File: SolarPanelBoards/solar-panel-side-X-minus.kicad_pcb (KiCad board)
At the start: 2 copper layers, 82 x 99 mm, 24 parts, among them J1 Conn_01x06, U1 OPT3001DNPT

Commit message: rearranged x-minus
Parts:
- moved C1 25.4 mm to (149.1, 79.8)
- moved U1 25.4 mm to (154.2, 79.8)
- moved SC1 9.67 mm to (126.6, 61.4), turned to 90 degrees
- moved SC2 9.39 mm to (176.9, 61.1), turned to 90 degrees
- moved D5 6.47 mm to (113.1, 118.6)
- moved D4 5.96 mm to (189.3, 119.8)
- moved SC4 5.68 mm to (168.8, 120.0), turned to 180 degrees
- moved SC5 5.68 mm to (133.2, 120.0), turned to 0 degrees
- moved SC3 5.40 mm to (168.8, 97.5), turned to 180 degrees
- moved SC6 5.40 mm to (133.3, 97.5), turned to 0 degrees
- moved D9 5.32 mm to (140.2, 81.8)
- moved D1 4.57 mm to (143.5, 81.9)
- moved D2 4.17 mm to (163.2, 82.4)
- moved J1 1.47 mm to (124.8, 59.9)
- moved D3 1.39 mm to (189.4, 102.1)
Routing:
- net Net-(D4-Pad2): track 78.5 -> 17.0 mm
- net Net-(D3-Pad2): track 30.3 -> 91.9 mm
- net SCL: track 42.0 -> 4.28 mm
- net GND: track 0.65 -> 31.8 mm, vias 16 -> 12
- net +3V3: track 29.9 -> 4.14 mm, vias 1 -> 0
- net VSOLAR: track 58.8 -> 83.8 mm, vias 1 -> 2
- net Net-(D2-Pad2): track 37.1 -> 18.1 mm
- net SDA: track 38.6 -> 20.2 mm
- net Net-(D1-Pad1): track 14.9 -> 0.00 mm, vias 0 -> 4
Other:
- outline, holes or cut-outs redrawn
- net class Default removed

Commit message: new coils
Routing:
- net VSOLAR: track 83.8 -> 39658.4 mm, vias 2 -> 15
- net Net-(D4-Pad2): track 17.0 -> 33.4 mm
- net Net-(D3-Pad2): track 91.9 -> 83.5 mm
- net Net-(D5-Pad2): track 30.3 -> 22.2 mm
- net Net-(D1-Pad1): vias 4 -> 0
- net GND: vias 12 -> 6
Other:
- copper layers 2 -> 6

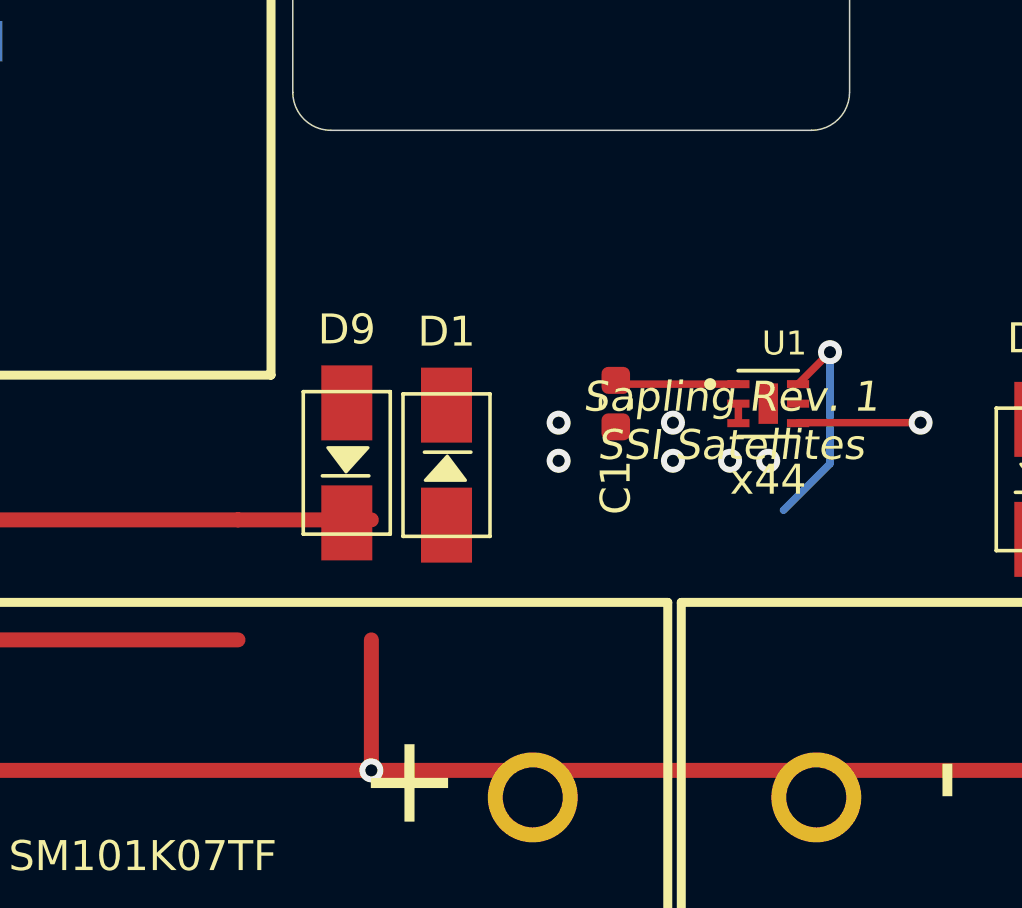
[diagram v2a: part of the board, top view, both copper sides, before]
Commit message: added I2C protection PCB layout
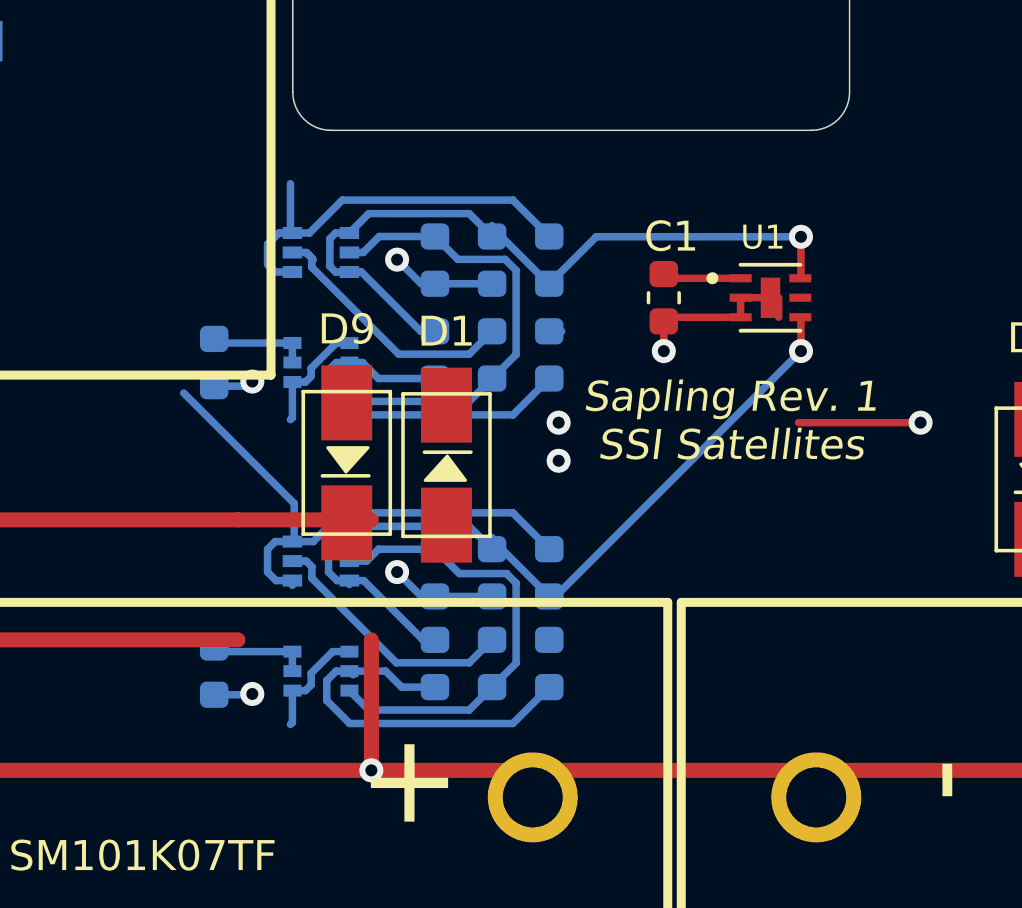
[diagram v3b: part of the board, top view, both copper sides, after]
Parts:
- added C2: 10nF, Capacitor_SMD:C_0603_1608Metric, B.Cu at (146.9, 88.5)
- added C3: 10nF, Capacitor_SMD:C_0603_1608Metric, B.Cu at (146.9, 78.2)
- added Q1: MBT2222ADW1T1, Package_TO_SOT_SMD:SOT-363_SC-70-6, B.Cu at (139.3, 85.1)
- added Q2: MBT2222ADW1T1, Package_TO_SOT_SMD:SOT-363_SC-70-6, B.Cu at (139.3, 74.8)
- added Q3: BSS138DWQ-7, mainboard:BSS138DWQ-7, B.Cu at (139.3, 88.8)
- added Q4: BSS138DWQ-7, mainboard:BSS138DWQ-7, B.Cu at (139.3, 78.5)
- added R1: 10K, Resistor_SMD:R_0603_1608Metric, B.Cu at (143.1, 85.5)
- added R10: 200K, Resistor_SMD:R_0603_1608Metric, B.Cu at (143.1, 78.2)
- added R11: 0, Resistor_SMD:R_0603_1608Metric, B.Cu at (146.9, 85.5)
- added R12: 0, Resistor_SMD:R_0603_1608Metric, B.Cu at (146.9, 75.1)
- added R2: 10K, Resistor_SMD:R_0603_1608Metric, B.Cu at (143.1, 75.1)
- added R3: 10K, Resistor_SMD:R_0603_1608Metric, B.Cu at (145.0, 85.5)
- added R4: 10K, Resistor_SMD:R_0603_1608Metric, B.Cu at (145.0, 75.1)
- added R5: 680, Resistor_SMD:R_0603_1608Metric, B.Cu at (145.0, 88.5)
- added R6: 680, Resistor_SMD:R_0603_1608Metric, B.Cu at (145.0, 78.2)
- added R7: 100K, Resistor_SMD:R_0603_1608Metric, B.Cu at (135.7, 88.8)
- added R8: 100K, Resistor_SMD:R_0603_1608Metric, B.Cu at (135.7, 78.5)
- added R9: 200K, Resistor_SMD:R_0603_1608Metric, B.Cu at (143.1, 88.5)
- moved C1 3.88 mm to (150.7, 76.3)
- moved U1 3.53 mm to (154.3, 76.3)
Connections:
- U1 pad 4: SCL -> (no net)
- U1 pad 6: SDA -> (no net)
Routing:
- net (no net): track 0.00 -> 135.0 mm, vias 0 -> 2
- net SCL: track 4.28 -> 23.2 mm
- net GND: track 31.8 -> 45.4 mm, vias 6 -> 3
- net +3V3: track 4.14 -> 13.5 mm, vias 0 -> 4
- net SDA: track 20.2 -> 26.6 mm, vias 1 -> 0
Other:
- board text added: "BYP"
- board text added: "DNP"
- board text removed: "x44"

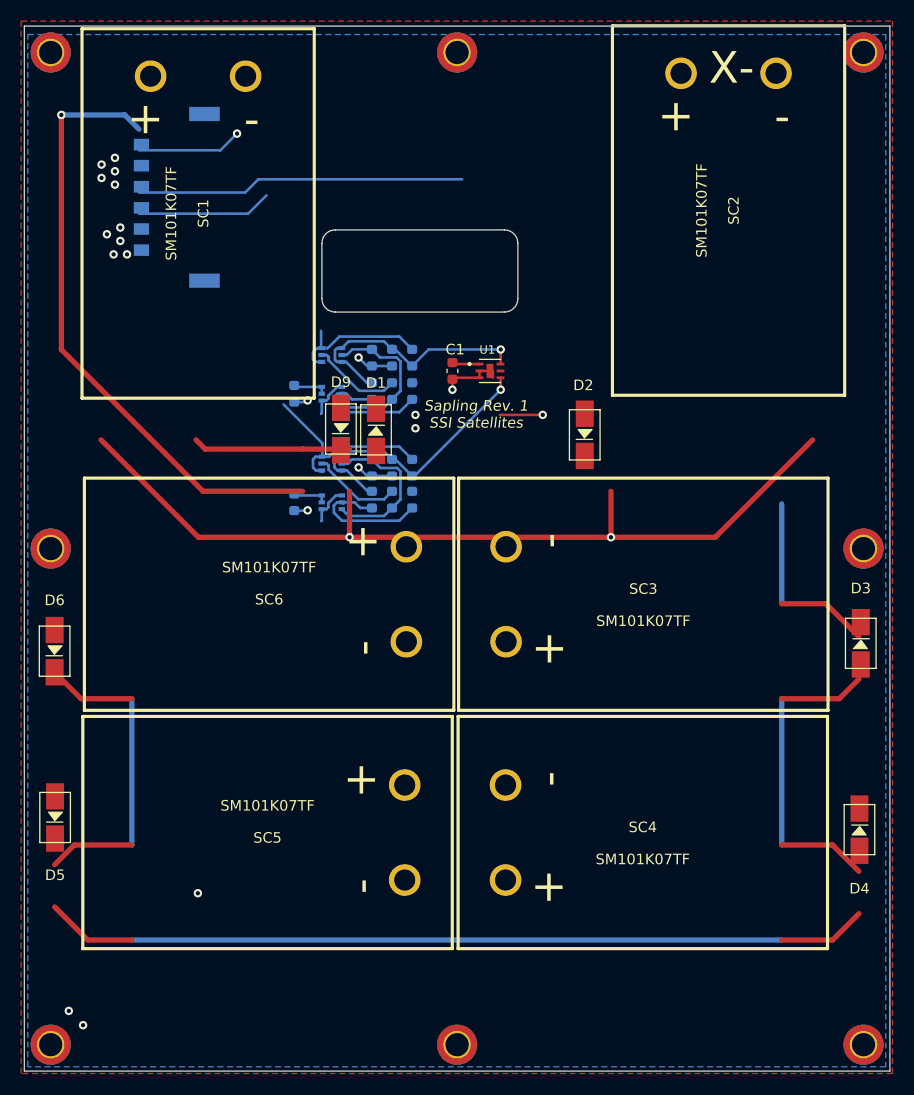
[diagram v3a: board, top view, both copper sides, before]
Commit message: New X-minus board w/ magnetorquer coils and H-bridge, I2C protection circuit
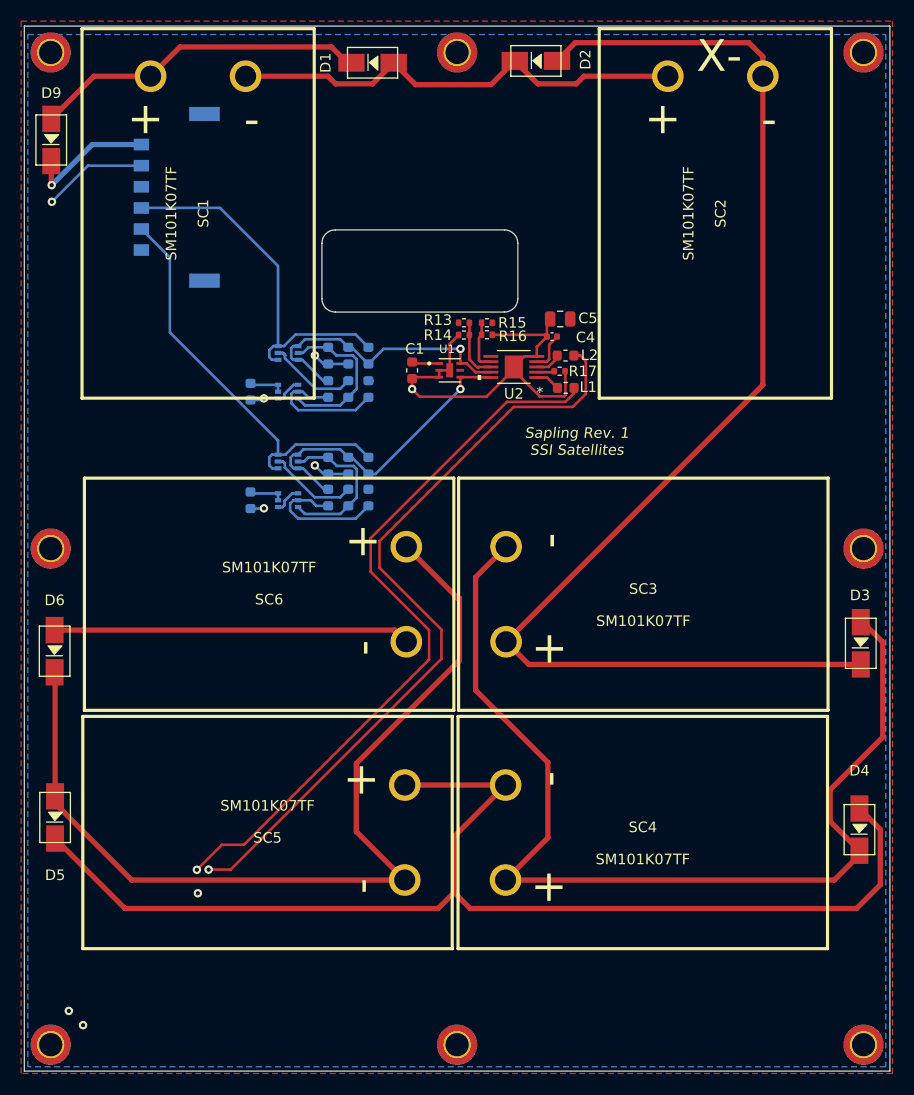
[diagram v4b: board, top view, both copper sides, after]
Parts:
- added C4: 0.1uF, Capacitor_SMD:C_0402_1005Metric, F.Cu at (160.2, 73.1)
- added C5: 10uF, Capacitor_SMD:C_0805_2012Metric, F.Cu at (160.9, 71.4)
- added L1: TBD, Inductor_SMD:L_0603_1608Metric, F.Cu at (161.4, 77.9)
- added L2: TBD, Inductor_SMD:L_0603_1608Metric, F.Cu at (161.4, 74.9)
- added R13: 0, Resistor_SMD:R_0402_1005Metric, F.Cu at (151.8, 71.8)
- added R14: 0, Resistor_SMD:R_0402_1005Metric, F.Cu at (151.8, 72.9)
- added R15: 0, Resistor_SMD:R_0402_1005Metric, F.Cu at (154.0, 71.8)
- added R16: 0, Resistor_SMD:R_0402_1005Metric, F.Cu at (154.0, 72.9)
- added R17: 0, Resistor_SMD:R_0402_1005Metric, F.Cu at (160.9, 76.3)
- added U2: DRV8830DGQR, sapling:DRV8830DGQ, F.Cu at (156.5, 75.9)
- R10, R9: value 200K -> 100K
- R5, R6: value 680 -> 600
- R7, R8: value 100K -> 10K
- moved D9 38.8 mm to (112.7, 54.4)
- moved D2 35.7 mm to (158.6, 47.0), turned to 0 degrees
- moved D1 34.8 mm to (143.2, 47.1), turned to 0 degrees
- moved Q1 4.15 mm to (135.1, 84.9)
- moved Q2 4.15 mm to (135.1, 74.6)
- moved Q3 4.15 mm to (135.1, 88.6)
- moved Q4 4.15 mm to (135.1, 78.3)
- moved C2 4.15 mm to (142.8, 88.3)
- moved C3 4.15 mm to (142.8, 78.0)
- moved R1 4.15 mm to (138.9, 85.3)
- moved R10 4.15 mm to (138.9, 78.0), turned to 90 degrees
- moved R11 4.15 mm to (142.8, 85.3), turned to -90 degrees
- moved R12 4.15 mm to (142.8, 74.9), turned to -90 degrees
- moved R2 4.15 mm to (138.9, 74.9)
- moved R3 4.15 mm to (140.9, 85.3), turned to -90 degrees
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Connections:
- C2 pad 1: (no net) -> Net-(C2-Pad1)
- C3 pad 1: (no net) -> Net-(C3-Pad1)
- J1 pad 4: SDA -> SDA1_b4iso
- J1 pad 5: SCL -> SCL1_b4iso
- J1 pad S1: (no net) -> unconnected-(J1-PadS1)
- J1 pad S2: (no net) -> unconnected-(J1-PadS2)
- Q1 pad 1: SCL -> SCL1_b4iso
- Q1 pad 2: (no net) -> Net-(Q1-Pad2)
- Q1 pad 3: SCL -> SCL1_b4iso
- Q1 pad 4: (no net) -> SCL
- Q1 pad 5: (no net) -> Net-(Q1-Pad5)
- Q1 pad 6: (no net) -> SCL
- Q2 pad 1: SDA -> SDA1_b4iso
- Q2 pad 2: (no net) -> Net-(Q2-Pad2)
- Q2 pad 3: SDA -> SDA1_b4iso
- Q2 pad 4: (no net) -> SDA
- Q2 pad 5: (no net) -> Net-(Q2-Pad5)
- Q2 pad 6: (no net) -> SDA
- Q3 pad 2: (no net) -> Net-(Q3-Pad2)
- Q3 pad 3: (no net) -> Net-(Q3-Pad2)
- Q3 pad 5: (no net) -> Net-(C2-Pad1)
- Q3 pad 6: (no net) -> Net-(Q1-Pad5)
- Q4 pad 2: (no net) -> Net-(Q4-Pad2)
- Q4 pad 3: (no net) -> Net-(Q4-Pad2)
- Q4 pad 5: (no net) -> Net-(C3-Pad1)
- Q4 pad 6: (no net) -> Net-(Q2-Pad5)
- R1 pad 2: (no net) -> Net-(Q1-Pad5)
- R10 pad 1: (no net) -> Net-(C3-Pad1)
- R10 pad 2: (no net) -> SDA
- R11 pad 1: (no net) -> SCL1_b4iso
- R12 pad 1: (no net) -> SDA1_b4iso
- R2 pad 2: (no net) -> Net-(Q2-Pad5)
- R3 pad 1: +3V3 -> SCL
- R3 pad 2: (no net) -> +3V3
- R4 pad 1: +3V3 -> SDA
- R4 pad 2: (no net) -> +3V3
- R5 pad 1: (no net) -> Net-(Q1-Pad5)
- R5 pad 2: (no net) -> Net-(Q1-Pad2)
- R6 pad 1: (no net) -> Net-(Q2-Pad2)
- R6 pad 2: (no net) -> Net-(Q2-Pad5)
- R7 pad 1: +3V3 -> Net-(Q3-Pad2)
- R7 pad 2: (no net) -> +3V3
- R8 pad 1: +3V3 -> Net-(Q4-Pad2)
- R8 pad 2: (no net) -> +3V3
- R9 pad 1: (no net) -> Net-(C2-Pad1)
- R9 pad 2: (no net) -> SCL
- U1 pad 4: (no net) -> SCL
- U1 pad 5: (no net) -> unconnected-(U1-Pad5)
- U1 pad 6: (no net) -> SDA
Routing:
- net /torque-coil: track 0.00 -> 39717.5 mm, vias 0 -> 5
- net VSOLAR: track 39658.4 -> 12.4 mm, vias 15 -> 1
- net (no net): track 135.0 -> 0.00 mm, vias 2 -> 0
- net Net-(D2-Pad2): track 18.1 -> 120.8 mm
- net Net-(D4-Pad2): track 33.4 -> 112.9 mm
- net Net-(D5-Pad2): track 22.2 -> 88.3 mm
- net Net-(D1-Pad2): track 83.8 -> 44.1 mm, vias 2 -> 0
- net SCL1_b4iso: track 0.00 -> 38.9 mm
- net SDA1_b4iso: track 0.00 -> 34.9 mm
- net GND: track 45.4 -> 80.1 mm, vias 3 -> 1
- net Net-(D1-Pad1): track 0.00 -> 31.9 mm
- net Net-(Q2-Pad5): track 0.00 -> 15.5 mm
- net Net-(Q1-Pad5): track 0.00 -> 15.3 mm
- net Net-(D3-Pad2): track 83.5 -> 98.0 mm
- net Net-(C2-Pad1): track 0.00 -> 12.9 mm
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- added copper zone on F.Cu, net +3V3
- removed copper zone on F.Cu, net GND

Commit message: X-minus board with backside component footprints fixed
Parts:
- C2, C3, J1, Q1, Q2, Q3, Q4, R1, R10, R11, R12, R2, R3, R4, R5, R6, R7, R8: moved to F.Cu
- turned C2 to -90 degrees
- turned C3 to -90 degrees
- turned J1 to -90 degrees
- turned Q1 to 180 degrees
- turned Q2 to 180 degrees
- turned Q3 to 180 degrees
- turned Q4 to 180 degrees
- turned R1 to -90 degrees
- turned R10 to -90 degrees
- turned R11 to 90 degrees
- turned R12 to 90 degrees
- turned R2 to -90 degrees
- turned R3 to 90 degrees
- turned R4 to 90 degrees
- turned R5 to -90 degrees
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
